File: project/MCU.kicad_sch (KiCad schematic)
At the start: 45 parts, among them IC301 ESDALC6V1W5, IC302 FAN5622SX, IC303 MX25U51245GZ4I00, IC304 TS3USB221A, IC305 NTS0104GU12, IC306 DRV2603RUNT, IC307 RV-8263-C8, M301 NORA-B106, M302 Vibration Motor, Q301 BC817W, Q302 PMZ550UNEYL, Q303 PMZ550UNEYL, X301 DOCK, X302 GC9A01A_CST816S

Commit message: Add KiCost
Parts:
- BZ301: Distributor Mouser -> (none); Mfr. CUI Devices -> (none); Mfr. No. CMT-322-65-SMT-TR -> (none); Order No. 490-CMT-322-65-SMTTR -> (none); manf (none) -> CUI Devices; manf# (none) -> CMT-322-65-SMT-TR; mouser# (none) -> 490-CMT-322-65-SMTTR
- C301: Distributor Mouser -> (none); Mfr. KYOCERA AVX -> (none); Mfr. No. 0603YC105JAT2A -> (none); Order No. 581-0603YC105JAT2A -> (none); manf (none) -> KYOCERA AVX; manf# (none) -> 0603YC105JAT2A; mouser# (none) -> 581-0603YC105JAT2A
- C302, C303, C304, C305, C306: Distributor Mouser -> (none); Mfr. KYOCERA AVX -> (none); Mfr. No. 06035C104KAT2A -> (none); Order No. 581-06035C104KAT2A -> (none); manf (none) -> KYOCERA AVX; manf# (none) -> 06035C104KAT2A; mouser# (none) -> 581-06035C104KAT2A
- C307: Distributor Mouser -> (none); Mfr. KYOCERA AVX -> (none); Mfr. No. 04025C104KAT2A -> (none); Order No. 581-04025C104KAT2A -> (none); manf (none) -> KYOCERA AVX; manf# (none) -> 04025C104KAT2A; mouser# (none) -> 581-04025C104KAT2A
- D301: Distributor Mouser -> (none); Mfr. Taiwan Semiconductor -> (none); Mfr. No. BAS316 RRG -> (none); Order No. 821-BAS316RRG -> (none); manf (none) -> Taiwan Semiconductor; manf# (none) -> BAS316 RRG; mouser# (none) -> 821-BAS316RRG
- D302: Distributor Mouser -> (none); Mfr. Wurth Elektronik -> (none); Mfr. No. 150060YS75003 -> (none); Order No. 710-150060YS75003 -> (none); manf (none) -> Wurth Elektronik; manf# (none) -> 150060YS75003; mouser# (none) -> 710-150060YS75003
- IC301: Distributor Mouser -> (none); Mfr. STMicroelectronics -> (none); Mfr. No. ESDALC6V1P5 -> (none); Order No. 511-ESDALC6V1P5 -> (none); manf (none) -> STMicroelectronics; manf# (none) -> ESDALC6V1P5; mouser# (none) -> 511-ESDALC6V1P5
- IC302: Distributor Mouser -> (none); Mfr. onsemi / Fairchild -> (none); Mfr. No. FAN5622SX -> (none); Order No. 512-FAN5622SX -> (none); manf (none) -> onsemi / Fairchild; manf# (none) -> FAN5622SX; mouser# (none) -> 512-FAN5622SX
- IC303: Distributor Mouser -> (none); Mfr. Macronix -> (none); Mfr. No. MX25U51245GZ4I00 -> (none); Order No. 95-25U51245GZ4I00T -> (none); manf (none) -> Macronix; manf# (none) -> MX25U51245GZ4I00; mouser# (none) -> 95-25U51245GZ4I00T
- IC304: Distributor Mouser -> (none); Mfr. Texas Instruments -> (none); Mfr. No. TS3USB221A -> (none); Order No. 595-TS3USB221A -> (none); manf (none) -> Texas Instruments; manf# (none) -> TS3USB221A; mouser# (none) -> 595-TS3USB221A
- IC305: Distributor Mouser -> (none); Mfr. NXP Semiconductors -> (none); Mfr. No. NTS0104GU12,115 -> (none); Order No. 771-NTS0104GU12115 -> (none); manf (none) -> NXP Semiconductors; manf# (none) -> NTS0104GU12,115; mouser# (none) -> 771-NTS0104GU12115
- IC306: Distributor Mouser -> (none); Mfr. Texas Instruments -> (none); Mfr. No. DRV2603RUNT -> (none); Order No. 595-DRV2603RUNT -> (none); manf (none) -> Texas Instruments; manf# (none) -> DRV2603RUNT; mouser# (none) -> 595-DRV2603RUNT
- IC307: Distributor Mouser -> (none); Mfr. Micro Crystal -> (none); Mfr. No. RV-8263-C8 32.768kHz-20PPM-TA-QA -> (none); Order No. 428-204291-MC01 -> (none); manf (none) -> Micro Crystal; manf# (none) -> RV-8263-C8 32.768kHz-20PPM-TA-QA; mouser# (none) -> 428-204291-MC01
- M301: Distributor Mouser -> (none); Mfr. u-blox -> (none); Mfr. No. NORA-B106-00B -> (none); Order No. 377-NORA-B106-00B -> (none); manf (none) -> u-blox; manf# (none) -> NORA-B106-00B; mouser# (none) -> 377-NORA-B106-00B
- M302: Distributor Digikey -> (none); Mfr. Vybronics Inc -> (none); Mfr. No. VZ30C1T8219732L -> (none); Order No. 1670-VZ30C1T8219732LCT-ND -> (none); manf (none) -> Vybronics Inc; manf# (none) -> VZ30C1T8219732L; mouser# (none) -> 1670-VZ30C1T8219732LCT-ND
- Q301: Distributor Mouser -> (none); Mfr. Nexperia -> (none); Mfr. No. BC817W,115 -> (none); Order No. 771-BC817W115 -> (none); manf (none) -> Nexperia; manf# (none) -> BC817W,115; mouser# (none) -> 771-BC817W115
- Q302, Q303: Distributor Mouser -> (none); Mfr. Nexperia -> (none); Mfr. No. PMZ550UNEYL -> (none); Order No. 771-PMZ550UNEYL -> (none); manf (none) -> Nexperia; manf# (none) -> PMZ550UNEYL; mouser# (none) -> 771-PMZ550UNEYL
- R301: Distributor Mouser -> (none); Mfr. YAGEO -> (none); Mfr. No. RC0603FR-0712KL -> (none); Order No. 603-RC0603FR-0712KL -> (none); manf (none) -> YAGEO; manf# (none) -> RC0603FR-0712KL; mouser# (none) -> 603-RC0603FR-0712KL
- R302, R305: Distributor Mouser -> (none); Mfr. YAGEO -> (none); Mfr. No. RC0603FR-07100KL -> (none); Order No. 603-RC0603FR-07100KL -> (none); manf (none) -> YAGEO; manf# (none) -> RC0603FR-07100KL; mouser# (none) -> 603-RC0603FR-07100KL
- R303, R304: Distributor Mouser -> (none); Mfr. YAGEO -> (none); Mfr. No. RC0603FR-074K7L -> (none); Order No. -- verschiedene Werte -- -> (none); manf (none) -> YAGEO; manf# (none) -> RC0603FR-074K7L; mouser# (none) -> -- verschiedene Werte --
- R306, R310: Distributor Mouser -> (none); Mfr. Bourns -> (none); Mfr. No. CR0402-J/-000GLF -> (none); Order No. 652-CR0603-J/-000ELF -> (none); manf (none) -> Bourns; manf# (none) -> CR0402-J/-000GLF; mouser# (none) -> 652-CR0603-J/-000ELF
- R307: Distributor Mouser -> (none); Mfr. YAGEO -> (none); Mfr. No. RC0603FR-07150KL -> (none); Order No. 603-RC0603FR-07150KL -> (none); manf (none) -> YAGEO; manf# (none) -> RC0603FR-07150KL; mouser# (none) -> 603-RC0603FR-07150KL
- R308: Distributor Mouser -> (none); Mfr. YAGEO -> (none); Mfr. No. RC0603FR-07270RL -> (none); Order No. 603-RC0603FR-07270RL -> (none); manf (none) -> YAGEO; manf# (none) -> RC0603FR-07270RL; mouser# (none) -> 603-RC0603FR-07270RL
- R309, R313: Distributor Mouser -> (none); Mfr. YAGEO -> (none); Mfr. No. RC0402FR-074K7L -> (none); Order No. -- verschiedene Werte -- -> (none); manf (none) -> YAGEO; manf# (none) -> RC0402FR-074K7L; mouser# (none) -> -- verschiedene Werte --
- R311: Distributor Mouser -> (none); Mfr. YAGEO -> (none); Mfr. No. RC0603FR-07180RL -> (none); Order No. 603-RC0603FR-07180RL -> (none); manf (none) -> YAGEO; manf# (none) -> RC0603FR-07180RL; mouser# (none) -> 603-RC0603FR-07180RL
- R312: Distributor Mouser -> (none); Mfr. YAGEO -> (none); Mfr. No. RC0603FR-07100RL -> (none); Order No. 603-RC0603FR-07100RL -> (none); manf (none) -> YAGEO; manf# (none) -> RC0603FR-07100RL; mouser# (none) -> 603-RC0603FR-07100RL
- R314: Distributor Mouser -> (none); Mfr. YAGEO -> (none); Mfr. No. RT0603FRE07220RL -> (none); Order No. 603-RT0603FRE07220RL -> (none); manf (none) -> YAGEO; manf# (none) -> RT0603FRE07220RL; mouser# (none) -> 603-RT0603FRE07220RL
- R401: Distributor Mouser -> (none); Mfr. YAGEO -> (none); Mfr. No. RC0603FR-100RL -> (none); Order No. 603-RC0603FR-100RL -> (none); manf (none) -> YAGEO; manf# (none) -> RC0603FR-100RL; mouser# (none) -> 603-RC0603FR-100RL
- S301, S302, S303, S304: Distributor Mouser -> (none); Mfr. E-Switch -> (none); Mfr. No. TL6340AF160Q -> (none); Order No. 612-TL6340AF160Q -> (none); manf (none) -> E-Switch; manf# (none) -> TL6340AF160Q; mouser# (none) -> 612-TL6340AF160Q
- X301: Mfr. Pomagtor -> (none); Mfr. No. RD90_LZH0230529-004_DJ-5PIN_PH2_54 -> (none); manf (none) -> Pomagtor; manf# (none) -> RD90_LZH0230529-004_DJ-5PIN_PH2_54
- X302: Mfr. EastRising -> (none); Mfr. No. OK-24F024-04 -> (none); manf (none) -> EastRising; manf# (none) -> OK-24F024-04

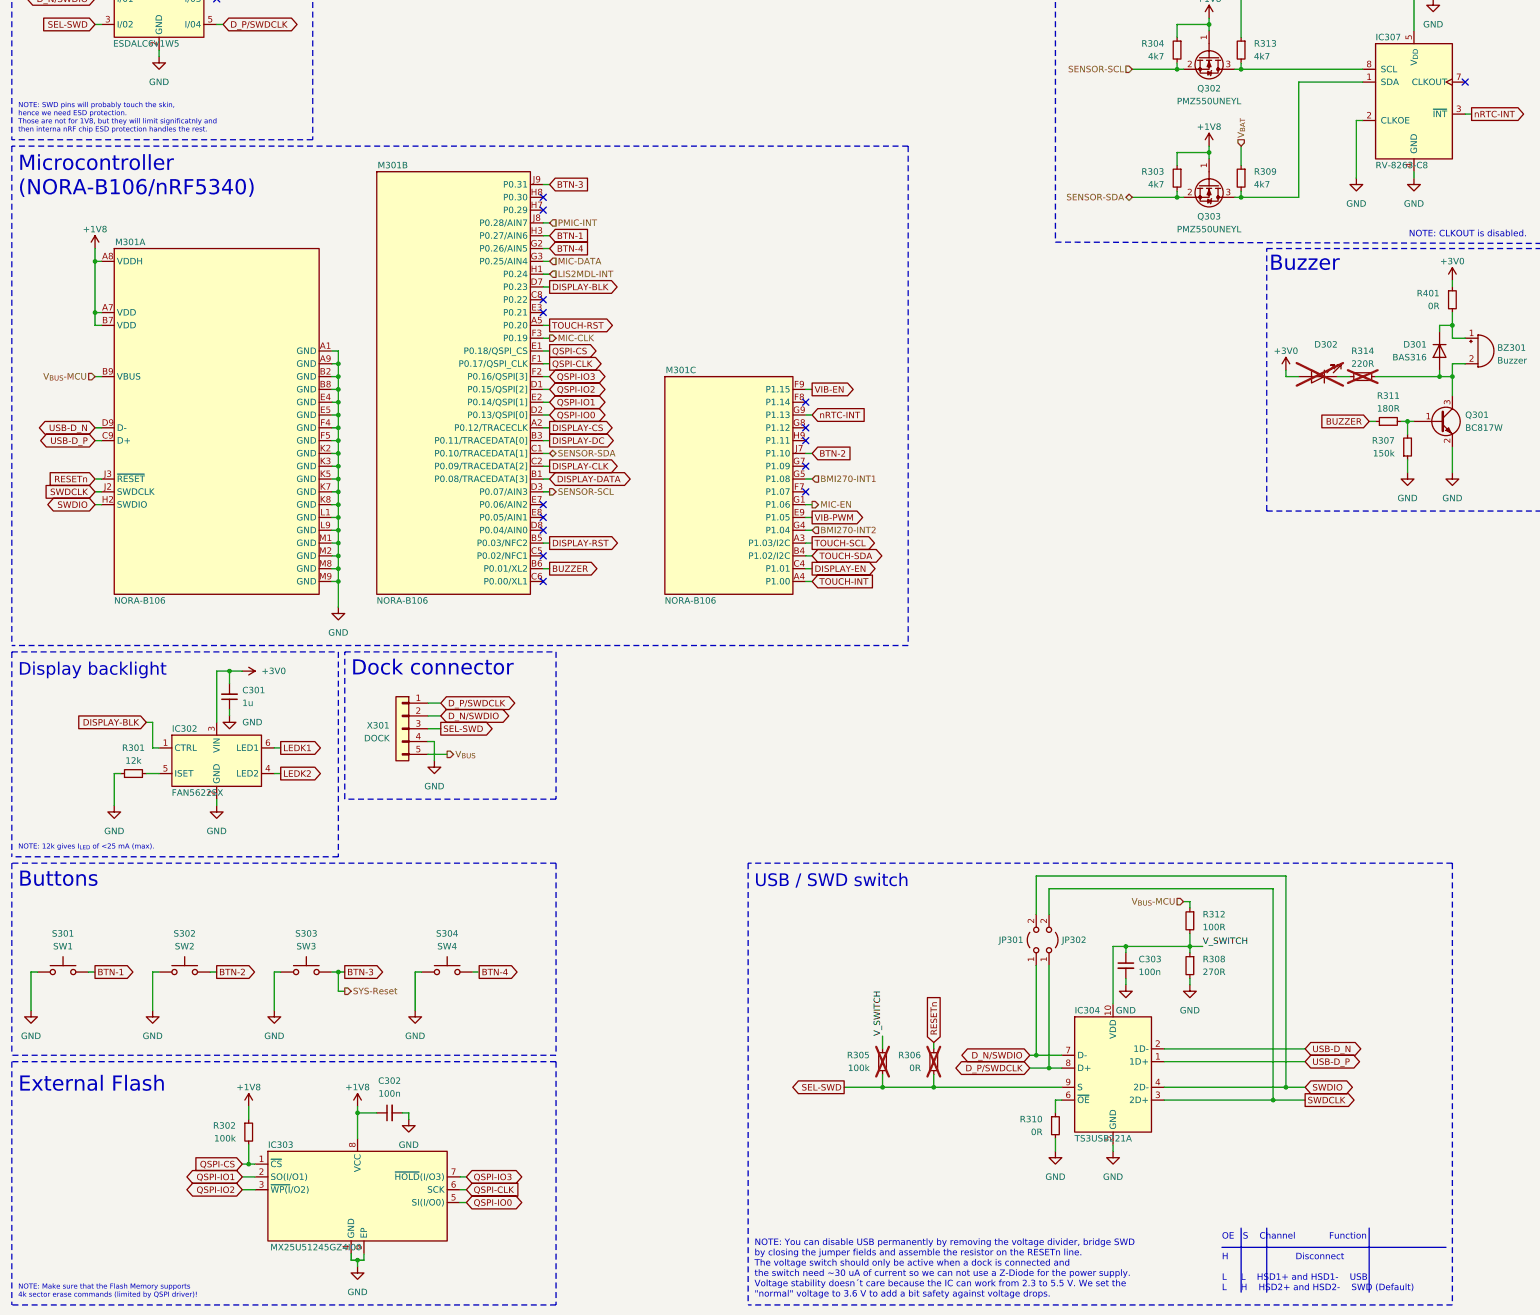
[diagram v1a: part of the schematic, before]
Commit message: Fix wrong part numbers
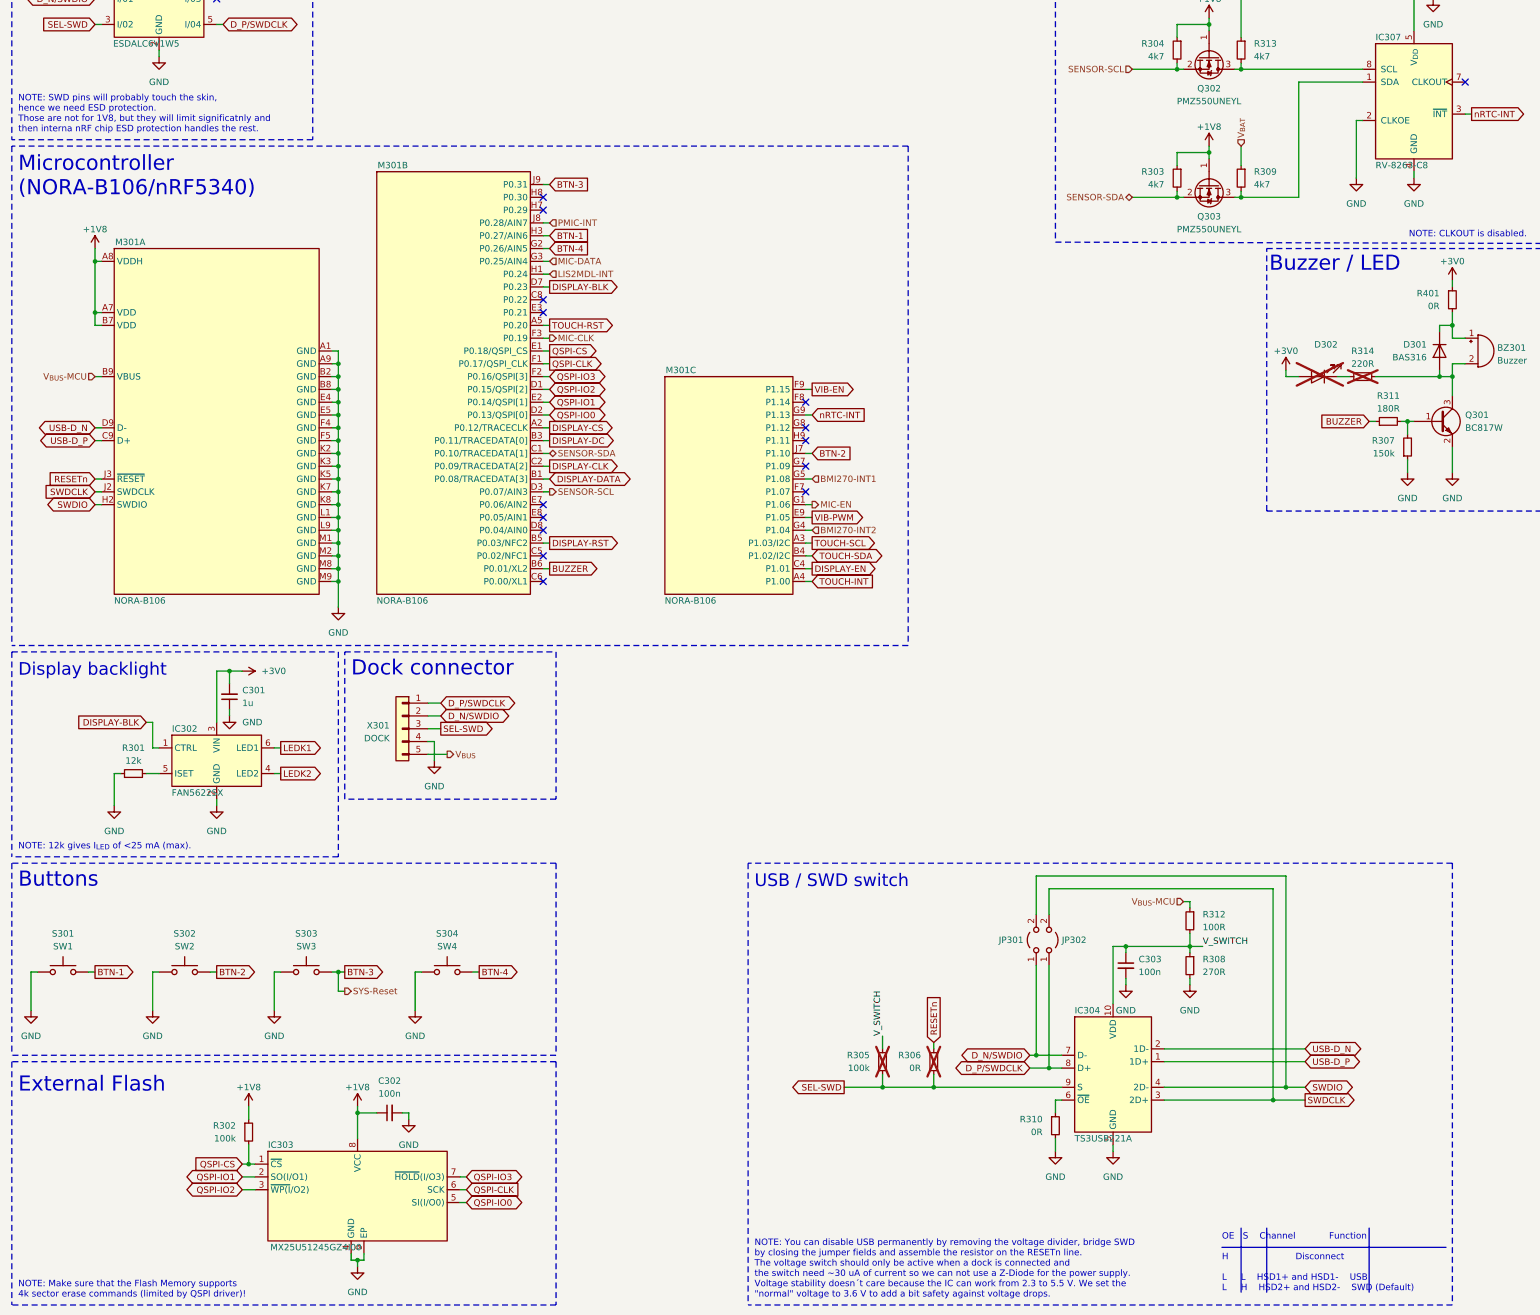
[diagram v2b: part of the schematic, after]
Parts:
- IC303: manf# MX25U51245GZ4I00 -> MX25U51245GZ4I00-TR; mouser# 95-25U51245GZ4I00T -> 95-25U51245GZ4I0TR
- R303, R304: mouser# -- verschiedene Werte -- -> 603-RC0603FR-074K7L
- R309, R313: mouser# -- verschiedene Werte -- -> 603-RC0402FR-074K7L
- S301, S302, S303, S304: manf# TL6340AF160Q -> TL6340AF160QG; mouser# 612-TL6340AF160Q -> 612-TL6340AF160QG
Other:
- note added: "Buzzer / LED"
- note removed: "Buzzer"
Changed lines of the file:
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@@
 		(effects
 			(font
-				(size 1 1)
+				(size 1.27 1.27)
 			)
 			(justify left bottom)
@@
 		)
 	)
-	(text "Buzzer"
+	(text "Buzzer / LED"
 		(exclude_from_sim no)
 		(at 262.128 79.756 0)
@@
 		(effects
 			(font
-				(size 1 1)
+				(size 1.27 1.27)
 			)
 			(justify left bottom)
@@
 		(effects
 			(font
-				(size 1 1)
+				(size 1.27 1.27)
 			)
 			(justify left bottom)
@@
 			)
 		)
-		(property "manf#" "TL6340AF160Q"
+		(property "manf#" "TL6340AF160QG"
 			(at 71.12 218.44 0)
 			(effects
@@
 			)
 		)
-		(property "mouser#" "612-TL6340AF160Q"
+		(property "mouser#" "612-TL6340AF160QG"
 			(at 71.12 218.44 0)
 			(effects
@@
 			)
 		)
-		(property "manf#" "TL6340AF160Q"
+		(property "manf#" "TL6340AF160QG"
 			(at 99.06 218.44 0)
 			(effects
@@
 			)
 		)
-		(property "mouser#" "612-TL6340AF160Q"
+		(property "mouser#" "612-TL6340AF160QG"
 			(at 99.06 218.44 0)
 			(effects
@@
 			)
 		)
-		(property "manf#" "TL6340AF160Q"
+		(property "manf#" "TL6340AF160QG"
 			(at 22.86 218.44 0)
 			(effects
@@
 			)
 		)
-		(property "mouser#" "612-TL6340AF160Q"
+		(property "mouser#" "612-TL6340AF160QG"
 			(at 22.86 218.44 0)
 			(effects
@@
 			)
 		)
-		(property "mouser#" "-- verschiedene Werte --"
+		(property "mouser#" "603-RC0402FR-074K7L"
 			(at 256.54 60.96 0)
 			(effects
@@
 			)
 		)
+		(property "mouser#" ""
+			(at 90.17 170.18 0)
+			(effects
+				(font
+					(size 1.27 1.27)
+				)
+				(hide yes)
+			)
+		)
 		(pin "1"
 		)
@@
 			)
 		)
-		(property "manf#" "TL6340AF160Q"
+		(property "manf#" "TL6340AF160QG"
 			(at 46.99 218.44 0)
 			(effects
@@
 			)
 		)
-		(property "mouser#" "612-TL6340AF160Q"
+		(property "mouser#" "612-TL6340AF160QG"
 			(at 46.99 218.44 0)
 			(effects
@@
 			)
 		)
-		(property "mouser#" "-- verschiedene Werte --"
+		(property "mouser#" "603-RC0603FR-074K7L"
 			(at 243.84 60.96 0)
 			(effects
@@
 			)
 		)
-		(property "mouser#" "-- verschiedene Werte --"
+		(property "mouser#" "603-RC0402FR-074K7L"
 			(at 256.54 35.56 0)
 			(effects
@@
 			)
 		)
-		(property "mouser#" "-- verschiedene Werte --"
+		(property "mouser#" "603-RC0603FR-074K7L"
 			(at 243.84 35.56 0)
 			(effects
@@
 			)
 		)
-		(property "manf#" "MX25U51245GZ4I00"
+		(property "manf#" "MX25U51245GZ4I00-TR"
 			(at 81.28 262.89 0)
 			(effects
@@
 			)
 		)
-		(property "mouser#" "95-25U51245GZ4I00T"
+		(property "mouser#" "95-25U51245GZ4I0TR"
 			(at 81.28 262.89 0)
 			(effects
